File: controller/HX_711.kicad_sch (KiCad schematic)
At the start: 30 parts, among them J1 M05PTH, Q1 MMBT4403, U1 HX711HX711, U7 OSHW-LOGOS

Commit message: finished ICM
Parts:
- removed JP2: M02PTH, SparkFun_HX711_Load_Cell:1X02, symbol SparkFun_HX711_Load_Cell-eagle-import:M02PTH
- added R31, R32: 10k, SparkFun_HX711_Load_Cell:0603-RES, symbol SparkFun_HX711_Load_Cell-eagle-import:20KOHM1/10W1%(0603)
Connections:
- net GND: now also R31.2, R32.2
- net B+: no longer names the net of U1.10 (INB+)
- net B+: now also R31.1
- net B-: no longer names the net of U1.9 (INB-)
- net B-: now also R32.1
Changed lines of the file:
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@@
     (stroke (width 0.1524) (type solid))
   )
-  (wire (pts (xy 189.23 109.22) (xy 191.77 109.22))
-    (stroke (width 0.1524) (type solid))
-  )
-  (wire (pts (xy 191.77 109.22) (xy 191.77 132.08))
+  (wire (pts (xy 189.23 109.22) (xy 199.39 109.22))
     (stroke (width 0.1524) (type solid))
   )
@@
     (stroke (width 0.1524) (type solid))
   )
-  (wire (pts (xy 82.55 134.62) (xy 82.55 99.06))
-    (stroke (width 0.1524) (type solid))
-  )
   (wire (pts (xy 194.31 71.12) (xy 194.31 78.74))
     (stroke (width 0.1524) (type solid))
@@
   )
   (wire (pts (xy 189.23 83.82) (xy 194.31 83.82))
-    (stroke (width 0.1524) (type solid))
-  )
-  (wire (pts (xy 194.31 134.62) (xy 82.55 134.62))
     (stroke (width 0.1524) (type solid))
   )
@@
     (stroke (width 0.1524) (type solid))
   )
-  (wire (pts (xy 191.77 132.08) (xy 85.09 132.08))
-    (stroke (width 0.1524) (type solid))
-  )
   (wire (pts (xy 201.93 83.82) (xy 201.93 86.36))
     (stroke (width 0.1524) (type solid))
@@
     (stroke (width 0.2032) (type solid))
   )
-  (wire (pts (xy 85.09 96.52) (xy 74.93 96.52))
-    (stroke (width 0.1524) (type solid))
-  )
   (wire (pts (xy 201.93 58.42) (xy 201.93 55.88))
     (stroke (width 0.1524) (type solid))
@@
     (stroke (width 0.1524) (type solid))
   )
-  (wire (pts (xy 82.55 99.06) (xy 74.93 99.06))
-    (stroke (width 0.1524) (type solid))
-  )
   (wire (pts (xy 222.25 99.06) (xy 219.71 99.06))
     (stroke (width 0.1524) (type solid))
@@
     (stroke (width 0.1524) (type solid))
   )
-  (wire (pts (xy 189.23 104.14) (xy 194.31 104.14))
+  (wire (pts (xy 189.23 104.14) (xy 199.39 104.14))
     (stroke (width 0.1524) (type solid))
   )
@@
     (stroke (width 0.1524) (type solid))
   )
-  (wire (pts (xy 194.31 104.14) (xy 194.31 134.62))
-    (stroke (width 0.1524) (type solid))
-  )
   (wire (pts (xy 189.23 99.06) (xy 194.31 99.06))
     (stroke (width 0.1524) (type solid))
@@
     (stroke (width 0.1524) (type solid))
   )
-  (wire (pts (xy 85.09 132.08) (xy 85.09 96.52))
-    (stroke (width 0.1524) (type solid))
-  )
   (text "AVDD = VBG(R1+R2)/R2" (at 75.692 68.834 0)
     (effects (font (size 1.778 1.5113)) (justify left bottom))
   )
-  (text "Default: Closed - Data rate set to 10SPS" (at 204.47 73.66 0)
+  (text "Default: Closed - Data rate set to 10SPS" (at 209.55 72.39 0)
     (effects (font (size 1.778 1.5113)) (justify left bottom))
   )
   (text "VCC vs VDD:\nVCC is the main supply voltage, while VDD sets the\ndigital logic voltage reference and should be\nconnected to microcontroller supply voltage, or\nshorted to VCC."
-    (at 201.93 127 0)
+    (at 203.2 133.35 0)
     (effects (font (size 1.778 1.5113)) (justify left bottom))
   )
@@
   )
   (text "Open jumper to set to 80SPS\nIncreases noise per read"
-    (at 204.47 78.74 0)
+    (at 209.55 77.47 0)
     (effects (font (size 1.778 1.5113)) (justify left bottom))
   )
@@
     (effects (font (size 1.2446 1.2446)) (justify left bottom))
   )
-  (label "B-" (at 80.01 96.52 0) (fields_autoplaced)
-    (effects (font (size 1.2446 1.2446)) (justify left bottom))
-  )
   (label "DAT" (at 214.63 93.98 0) (fields_autoplaced)
     (effects (font (size 1.2446 1.2446)) (justify left bottom))
@@
     (effects (font (size 1.2446 1.2446)) (justify left bottom))
   )
-  (label "B+" (at 80.01 99.06 0) (fields_autoplaced)
-    (effects (font (size 1.2446 1.2446)) (justify left bottom))
-  )
   (label "A-" (at 80.01 78.74 0) (fields_autoplaced)
     (effects (font (size 1.2446 1.2446)) (justify left bottom))
@@
     )
   )
+  (symbol (lib_id "SparkFun_HX711_Load_Cell-eagle-import:20KOHM1/10W1%(0603)") (at 204.47 104.14 0) (unit 1)
+    (in_bom yes) (on_board yes) (dnp no)
+    (property "Reference" "R31" (at 200.66 102.6414 0)
+      (effects (font (size 1.778 1.5113)) (justify left bottom))
+    )
+    (property "Value" "10k" (at 200.66 107.442 0)
+      (effects (font (size 1.778 1.5113)) (justify left bottom))
+    )
+    (property "Footprint" "SparkFun_HX711_Load_Cell:0603-RES" (at 204.47 104.14 0)
+      (effects (font (size 1.27 1.27)) hide)
+    )
+    (property "Datasheet" "" (at 204.47 104.14 0)
+      (effects (font (size 1.27 1.27)) hide)
+    )
+    (pin "2")
+    (pin "1")
+    (instances
+      (project "Adafruit HUZZAH32 ESP32 Feather"
+        (path "/3caf2dbf-4164-474d-8386-d91904ea6b76/d80eb16a-130c-4dac-9caa-70b8cea5979f"
+          (reference "R31") (unit 1)
+        )
+      )
+    )
+  )
   (symbol (lib_id "SparkFun_HX711_Load_Cell-eagle-import:REVISION") (at 170.18 191.262 0) (unit 1)
     (in_bom yes) (on_board yes) (dnp no)
@@
     )
   )
+  (symbol (lib_id "SparkFun_HX711_Load_Cell-eagle-import:GND") (at 209.55 111.76 0) (unit 1)
+    (in_bom yes) (on_board yes) (dnp no)
+    (property "Reference" "#GND01" (at 209.55 111.76 0)
+      (effects (font (size 1.27 1.27)) hide)
+    )
+    (property "Value" "GND" (at 207.01 114.3 0)
+      (effects (font (size 1.778 1.5113)) (justify left bottom))
+    )
+    (property "Footprint" "" (at 209.55 111.76 0)
+      (effects (font (size 1.27 1.27)) hide)
+    )
+    (property "Datasheet" "" (at 209.55 111.76 0)
+      (effects (font (size 1.27 1.27)) hide)
+    )
+    (pin "1")
+    (instances
+      (project "Adafruit HUZZAH32 ESP32 Feather"
+        (path "/3caf2dbf-4164-474d-8386-d91904ea6b76/d80eb16a-130c-4dac-9caa-70b8cea5979f"
+          (reference "#GND01") (unit 1)
+        )
+      )
+    )
+  )
   (symbol (lib_id "SparkFun_HX711_Load_Cell-eagle-import:SFE_LOGO_NAME_FLAME.1_INCH") (at 82.55 195.58 0) (unit 1)
     (in_bom yes) (on_board yes) (dnp no)
@@
     )
     (property "Value" "GND" (at 95.25 91.44 0)
-      (effects (font (size 1.778 1.5113)) (justify left bottom))
+      (effects (font (size 1.778 1.5113)) (justify right bottom))
     )
     (property "Footprint" "" (at 97.79 88.9 0)
@@
     )
   )
+  (symbol (lib_id "SparkFun_HX711_Load_Cell-eagle-import:20KOHM1/10W1%(0603)") (at 204.47 109.22 0) (unit 1)
+    (in_bom yes) (on_board yes) (dnp no)
+    (property "Reference" "R32" (at 196.85 107.95 0)
+      (effects (font (size 1.778 1.5113)) (justify left bottom))
+    )
+    (property "Value" "10k" (at 200.66 112.522 0)
+      (effects (font (size 1.778 1.5113)) (justify left bottom))
+    )
+    (property "Footprint" "SparkFun_HX711_Load_Cell:0603-RES" (at 204.47 109.22 0)
+      (effects (font (size 1.27 1.27)) hide)
+    )
+    (property "Datasheet" "" (at 204.47 109.22 0)
+      (effects (font (size 1.27 1.27)) hide)
+    )
+    (pin "2")
+    (pin "1")
+    (instances
+      (project "Adafruit HUZZAH32 ESP32 Feather"
+        (path "/3caf2dbf-4164-474d-8386-d91904ea6b76/d80eb16a-130c-4dac-9caa-70b8cea5979f"
+          (reference "R32") (unit 1)
+        )
+      )
+    )
+  )
   (symbol (lib_id "SparkFun_HX711_Load_Cell-eagle-import:FIDUCIAL1X2") (at 267.97 170.18 0) (unit 1)
     (in_bom yes) (on_board yes) (dnp no)
@@
         (path "/3caf2dbf-4164-474d-8386-d91904ea6b76/d80eb16a-130c-4dac-9caa-70b8cea5979f"
           (reference "STANDOFF1") (unit 1)
-        )
-      )
-    )
-  )
-  (symbol (lib_id "SparkFun_HX711_Load_Cell-eagle-import:M02PTH") (at 67.31 99.06 0) (unit 1)
-    (in_bom yes) (on_board yes) (dnp no)
-    (property "Reference" "JP2" (at 64.77 93.218 0)
-      (effects (font (size 1.778 1.5113)) (justify left bottom))
-    )
-    (property "Value" "M02PTH" (at 64.77 104.14 0)
-      (effects (font (size 1.778 1.5113)) (justify left bottom) hide)
-    )
-    (property "Footprint" "SparkFun_HX711_Load_Cell:1X02" (at 67.31 99.06 0)
-      (effects (font (size 1.27 1.27)) hide)
-    )
-    (property "Datasheet" "" (at 67.31 99.06 0)
-      (effects (font (size 1.27 1.27)) hide)
-    )
-    (pin "2")
-    (pin "1")
-    (instances
-      (project "SparkFun_HX711_Load_Cell"
-        (path "/1331fc83-31fc-4736-9918-4924b73c6a6e"
-          (reference "JP2") (unit 1)
-        )
-      )
-      (project "Adafruit HUZZAH32 ESP32 Feather"
-        (path "/3caf2dbf-4164-474d-8386-d91904ea6b76/d80eb16a-130c-4dac-9caa-70b8cea5979f"
-          (reference "JP8") (unit 1)
         )
       )
@@
         )
       )
+    )
+  )
+  (symbol (lib_id "SparkFun_HX711_Load_Cell-eagle-import:GND") (at 209.55 106.68 0) (unit 1)
+    (in_bom yes) (on_board yes) (dnp no)
+    (property "Reference" "#GND08" (at 209.55 106.68 0)
+      (effects (font (size 1.27 1.27)) hide)
+    )
+    (property "Value" "GND" (at 207.01 109.22 0)
+      (effects (font (size 1.778 1.5113)) (justify left bottom))
+    )
+    (property "Footprint" "" (at 209.55 106.68 0)
+      (effects (font (size 1.27 1.27)) hide)
+    )
+    (property "Datasheet" "" (at 209.55 106.68 0)
+      (effects (font (size 1.27 1.27)) hide)
+    )
+    (pin "1")
+    (instances
+      (project "Adafruit HUZZAH32 ESP32 Feather"
+        (path "/3caf2dbf-4164-474d-8386-d91904ea6b76/d80eb16a-130c-4dac-9caa-70b8cea5979f"
+          (reference "#GND08") (unit 1)
+        )
+      )

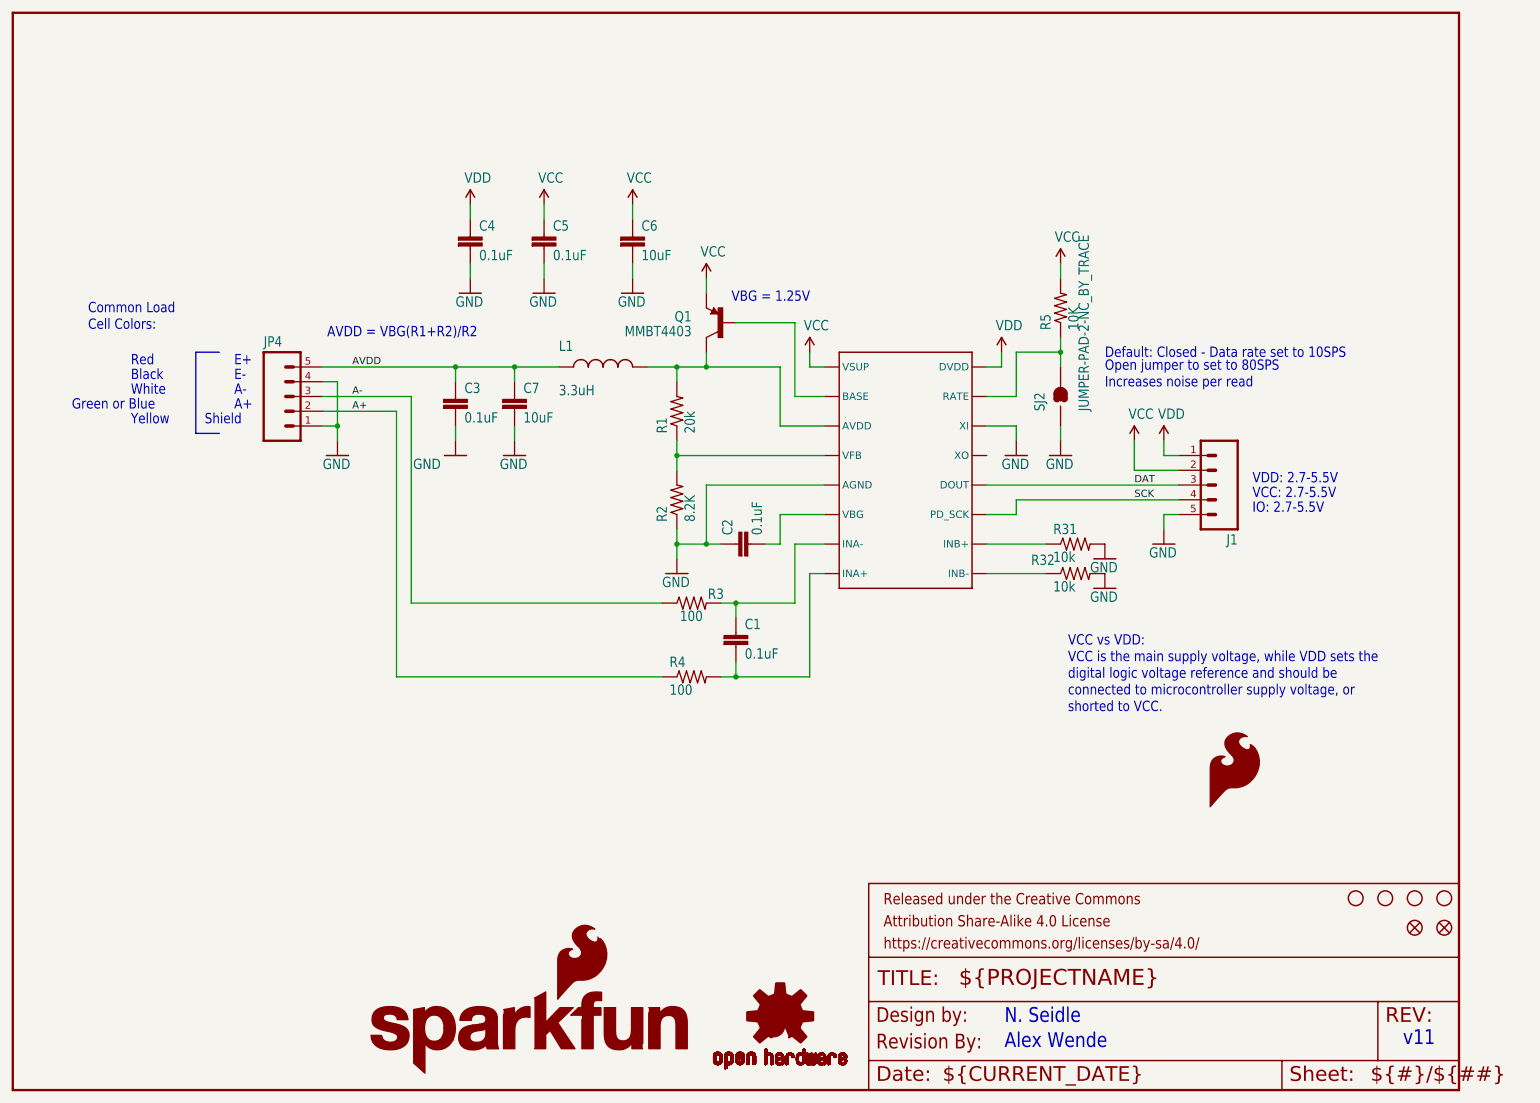
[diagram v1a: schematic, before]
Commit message: added open jumper
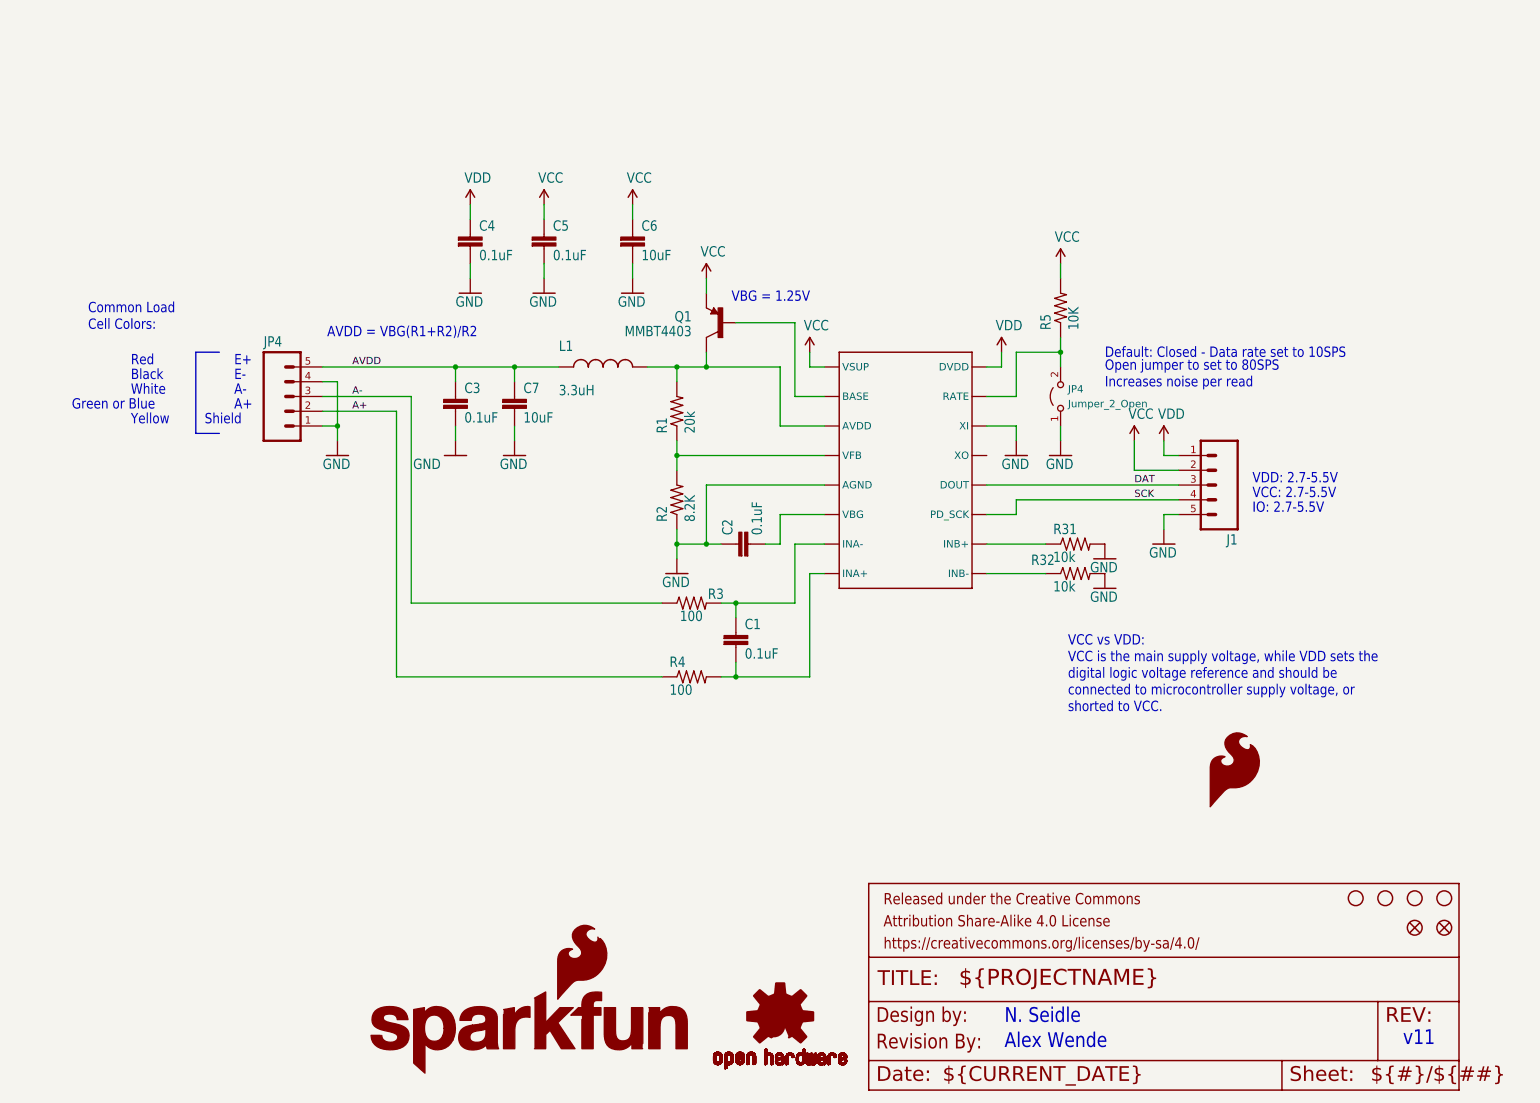
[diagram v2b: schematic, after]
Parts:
- removed unit 1 of FRAME1
- removed SJ2: JUMPER-PAD-2-NC_BY_TRACE, SparkFun_HX711_Load_Cell:PAD-JUMPER-2-NC_BY_TRACE_YES_SILK, symbol SparkFun_HX711_Load_Cell-eagle-import:JUMPER-PAD-2-NC_BY_TRACE
- added JP4: Jumper_2_Open, Jumper:SolderJumper-2_P1.3mm_Open_Pad1.0x1.5mm, symbol Jumper:Jumper_2_Open
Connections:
- net GND: now also JP4.1 (A)
- net at R5.1, U1.15 (RATE): now also JP4.2 (B)
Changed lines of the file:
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@@
+    )
+  )
+  (symbol (lib_id "Jumper:Jumper_2_Open") (at 201.93 78.74 90) (unit 1)
+    (in_bom yes) (on_board yes) (dnp no) (fields_autoplaced)
+    (property "Reference" "JP4" (at 203.2 77.47 90)
+      (effects (font (size 1.27 1.27)) (justify right))
+    )
+    (property "Value" "Jumper_2_Open" (at 203.2 80.01 90)
+      (effects (font (size 1.27 1.27)) (justify right))
+    )
+    (property "Footprint" "Jumper:SolderJumper-2_P1.3mm_Open_Pad1.0x1.5mm" (at 201.93 78.74 0)
+      (effects (font (size 1.27 1.27)) hide)
+    )
+    (property "Datasheet" "~" (at 201.93 78.74 0)
+      (effects (font (size 1.27 1.27)) hide)
+    )
+    (pin "1")
+    (pin "2")
+    (instances
+      (project "Adafruit HUZZAH32 ESP32 Feather"
+        (path "/3caf2dbf-4164-474d-8386-d91904ea6b76/d80eb16a-130c-4dac-9caa-70b8cea5979f"
+          (reference "JP4") (unit 1)
+        )
+      )
     )
   )
@@
     )
   )
-  (symbol (lib_id "SparkFun_HX711_Load_Cell-eagle-import:FRAME-LETTER") (at 21.59 198.12 0) (unit 1)
-    (in_bom yes) (on_board yes) (dnp no)
-    (property "Reference" "FRAME1" (at 21.59 198.12 0)
-      (effects (font (size 1.27 1.27)) hide)
-    )
-    (property "Value" "FRAME-LETTER" (at 21.59 198.12 0)
-      (effects (font (size 1.27 1.27)) hide)
-    )
-    (property "Footprint" "SparkFun_HX711_Load_Cell:CREATIVE_COMMONS" (at 21.59 198.12 0)
-      (effects (font (size 1.27 1.27)) hide)
-    )
-    (property "Datasheet" "" (at 21.59 198.12 0)
-      (effects (font (size 1.27 1.27)) hide)
-    )
-    (instances
-      (project "SparkFun_HX711_Load_Cell"
-        (path "/1331fc83-31fc-4736-9918-4924b73c6a6e"
-          (reference "FRAME1") (unit 1)
-        )
-      )
-      (project "Adafruit HUZZAH32 ESP32 Feather"
-        (path "/3caf2dbf-4164-474d-8386-d91904ea6b76/d80eb16a-130c-4dac-9caa-70b8cea5979f"
-          (reference "FRAME2") (unit 1)
-        )
-      )
-    )
-  )
   (symbol (lib_id "SparkFun_HX711_Load_Cell-eagle-import:GND") (at 209.55 111.76 0) (unit 1)
     (in_bom yes) (on_board yes) (dnp no)
@@
         )
       )
-    )
-  )
-  (symbol (lib_id "SparkFun_HX711_Load_Cell-eagle-import:JUMPER-PAD-2-NC_BY_TRACE") (at 201.93 78.74 90) (unit 1)
-    (in_bom yes) (on_board yes) (dnp no)
-    (property "Reference" "SJ2" (at 199.39 81.28 0)
-      (effects (font (size 1.778 1.5113)) (justify left bottom))
-    )
-    (property "Value" "JUMPER-PAD-2-NC_BY_TRACE" (at 207.01 81.28 0)
-      (effects (font (size 1.778 1.5113)) (justify left bottom))
-    )
-    (property "Footprint" "SparkFun_HX711_Load_Cell:PAD-JUMPER-2-NC_BY_TRACE_YES_SILK" (at 201.93 78.74 0)
-      (effects (font (size 1.27 1.27)) hide)
-    )
-    (property "Datasheet" "" (at 201.93 78.74 0)
-      (effects (font (size 1.27 1.27)) hide)
-    )
-    (pin "2")
-    (pin "1")
-    (instances
-      (project "SparkFun_HX711_Load_Cell"
-        (path "/1331fc83-31fc-4736-9918-4924b73c6a6e"
-          (reference "SJ2") (unit 1)
-        )
-      )
-      (project "Adafruit HUZZAH32 ESP32 Feather"
-        (path "/3caf2dbf-4164-474d-8386-d91904ea6b76/d80eb16a-130c-4dac-9caa-70b8cea5979f"
-          (reference "SJ1") (unit 1)
-        )
-      )
